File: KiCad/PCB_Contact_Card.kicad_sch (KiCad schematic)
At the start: 4 parts

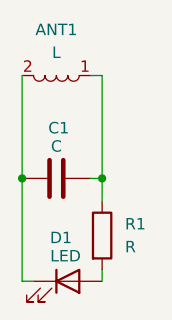
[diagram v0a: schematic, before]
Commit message: footprint fixed
アンテナのフットプリントのバク修正
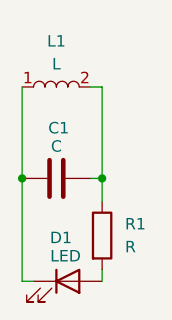
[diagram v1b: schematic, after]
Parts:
- removed ANT1: L, PCB_BusinessCard_lib:NFC_COIL_36.7x36.7_3uH, symbol NFC_COIL_36.7x36.7_3uH:L
- added L1: L, lib:NFC_COIL_36.7x36.7_3uH, symbol NFC_COIL_36.7x36.7_3uH:L
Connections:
- net at C1.2, R1.1: now also L1.2
- net at C1.1, D1.1 (K): now also L1.1
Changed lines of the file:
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@@
-	(wire
-		(pts
-			(xy 81.28 59.69) (xy 81.28 71.12)
-		)
-		(stroke
-			(width 0)
-			(type default)
-		)
-	)
-	(wire
-		(pts
-			(xy 81.28 59.69) (xy 80.01 59.69)
-		)
-		(stroke
-			(width 0)
-			(type default)
-		)
-	)
 	(wire
 		(pts
@@
 	(wire
 		(pts
-			(xy 72.39 59.69) (xy 72.39 71.12)
-		)
-		(stroke
-			(width 0)
-			(type default)
-		)
-	)
-	(wire
-		(pts
 			(xy 81.28 81.28) (xy 81.28 82.55)
 		)
@@
 	(wire
 		(pts
+			(xy 80.01 60.96) (xy 81.28 60.96)
+		)
+		(stroke
+			(width 0)
+			(type default)
+		)
+	)
+	(wire
+		(pts
 			(xy 81.28 71.12) (xy 81.28 73.66)
+		)
+		(stroke
+			(width 0)
+			(type default)
+		)
+	)
+	(wire
+		(pts
+			(xy 72.39 60.96) (xy 72.39 71.12)
+		)
+		(stroke
+			(width 0)
+			(type default)
+		)
+	)
+	(wire
+		(pts
+			(xy 81.28 60.96) (xy 81.28 71.12)
 		)
 		(stroke
@@
 	(symbol
 		(lib_id "NFC_COIL_36.7x36.7_3uH:L")
-		(at 76.2 59.69 0)
+		(at 76.2 60.96 180)
 		(unit 1)
 		(exclude_from_sim no)
@@
 		(dnp no)
 		(fields_autoplaced yes)
-		(property "Reference" "ANT1"
-			(at 76.2 54.61 0)
+		(property "Reference" "L1"
+			(at 76.2 55.88 0)
 			(effects
 				(font
@@
 		)
 		(property "Value" "L"
-			(at 76.2 57.15 0)
-			(effects
-				(font
-					(size 1.27 1.27)
-				)
-			)
-		)
-		(property "Footprint" "PCB_BusinessCard_lib:NFC_COIL_36.7x36.7_3uH"
-			(at 77.724 67.564 0)
+			(at 76.2 58.42 0)
+			(effects
+				(font
+					(size 1.27 1.27)
+				)
+			)
+		)
+		(property "Footprint" "lib:NFC_COIL_36.7x36.7_3uH"
+			(at 74.676 53.086 0)
 			(effects
 				(font
@@
 		)
 		(property "Datasheet" "~"
-			(at 76.2 59.69 90)
+			(at 76.2 60.96 90)
 			(effects
 				(font
@@
 		)
 		(property "Description" "NFC_COIL_36.7x36.7_3uH"
-			(at 76.454 62.992 0)
+			(at 75.946 57.658 0)
 			(do_not_autoplace yes)
 			(effects
@@
 			(project ""
 				(path "/bcec56eb-8771-4eb1-814f-551b472537c2"
-					(reference "ANT1")
+					(reference "L1")
 					(unit 1)
 				)
